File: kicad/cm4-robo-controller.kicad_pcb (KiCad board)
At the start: 4 copper layers, 150 x 90 mm, 254 parts, among them CN1 SMA-KWE_C7498154, J1 KF7620-7.62-2P, J10 KF2EDGR-2.54-2P, J11 KF7620-7.62-2P, J12 KF2EDGR-2.54-2P, J13 KF2EDGR-2.54-2P, J14 KF7620-7.62-2P, J15 PM254-2-12-Z-8.5, J16 PM254-2-09-Z-8.5, J2 HX PZ2.54-2X5P TP, J3 Header-Male-2.54_2x3, J4 2541WV-2X12P, J5 Header-Male-2.54_1x3, J6 Header-Male-2.54_2x3, J7 SMA-KWE_C7498154, J8 KF2EDGR-2.54-4P, J9 KF2EDGR-2.54-3P, Q1 SP40P04NK, Q2 DMP6023LE-13, Q3 NCE6008AS, Q4 BSS138, SW1 SS-12F49-G050, U1 74LVC1G07SE-7, U10 74LVC1G07SE-7, U11 MX26631DL, U12 MAX-M10S-00B, U13 74LVC1G17SE-7, U14 74LVC1G17SE-7, U15 AP64501SP-13, U16 74LVC1G17SE-7, U17 74LVC1G07SE-7, U18 TPS70933DBVR, U19 74LVC1G17SE-7, U2 FSUSB42MUX, U3 USB2514B-I/M2, U4 AP22653W6-7, U5 TPD4EUSB30DQAR, U6 TPD4EUSB30DQAR, U7 TPD4EUSB30DQAR, U8 TPD4EUSB30DQAR, U9 TPD4EUSB30DQAR, X1 24MHz

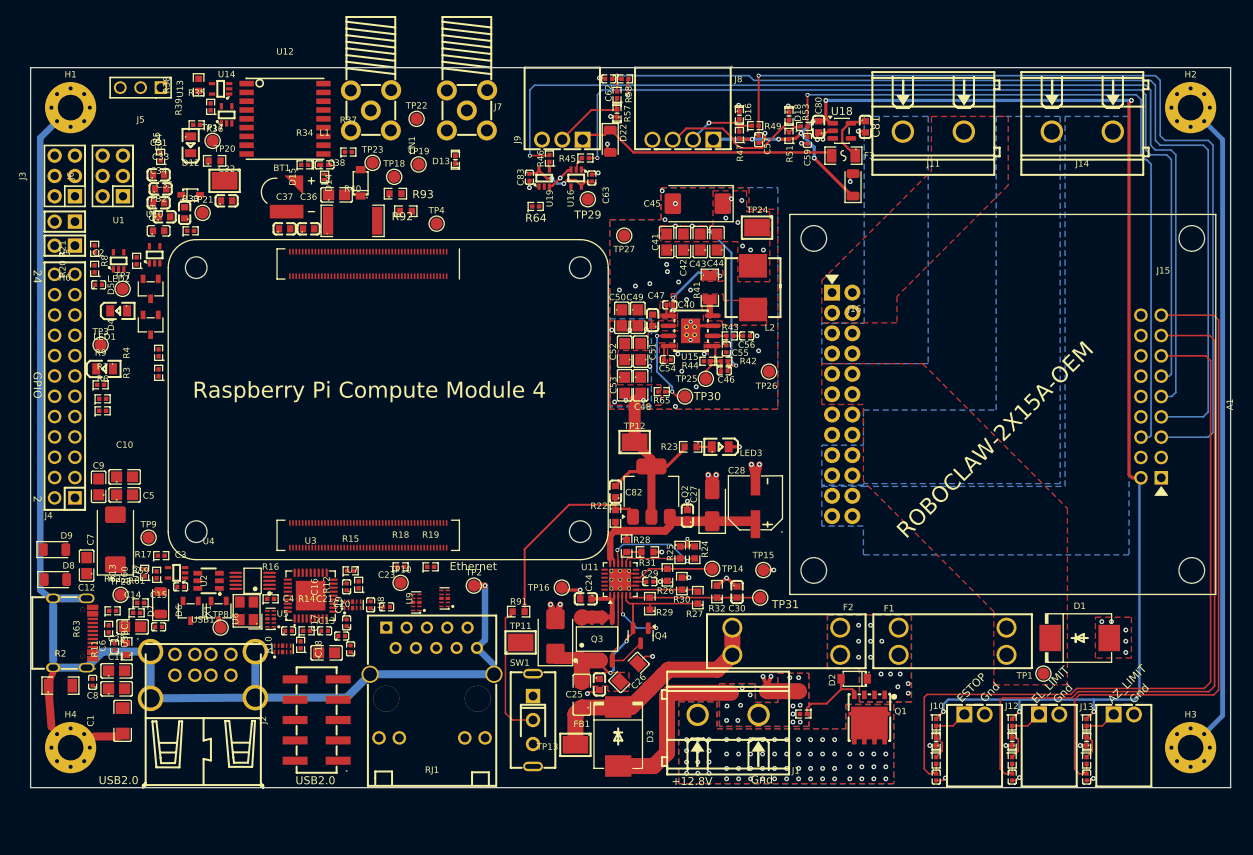
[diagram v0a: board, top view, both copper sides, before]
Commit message: PCB rework: rotate RoboClaw, battery input at top, planes redrawn, right half routed
- A1 rotated 90 CW and moved down; J14/J11 motor pours straight to the A1 pins
- J14 pins swapped (M2 polarity) in the schematic; J14 moved clear of D1
- Battery input, fuses and TVS diodes along the top edge; NT1 at J1-
- In1 (GND/PGND) and In2 (5V/V_MOTOR) split redrawn for the new layout
- Power block re-routed; 12V fed to the buck input on B.Cu
- UART buffers back on logic GND; RoboClaw signal section routed
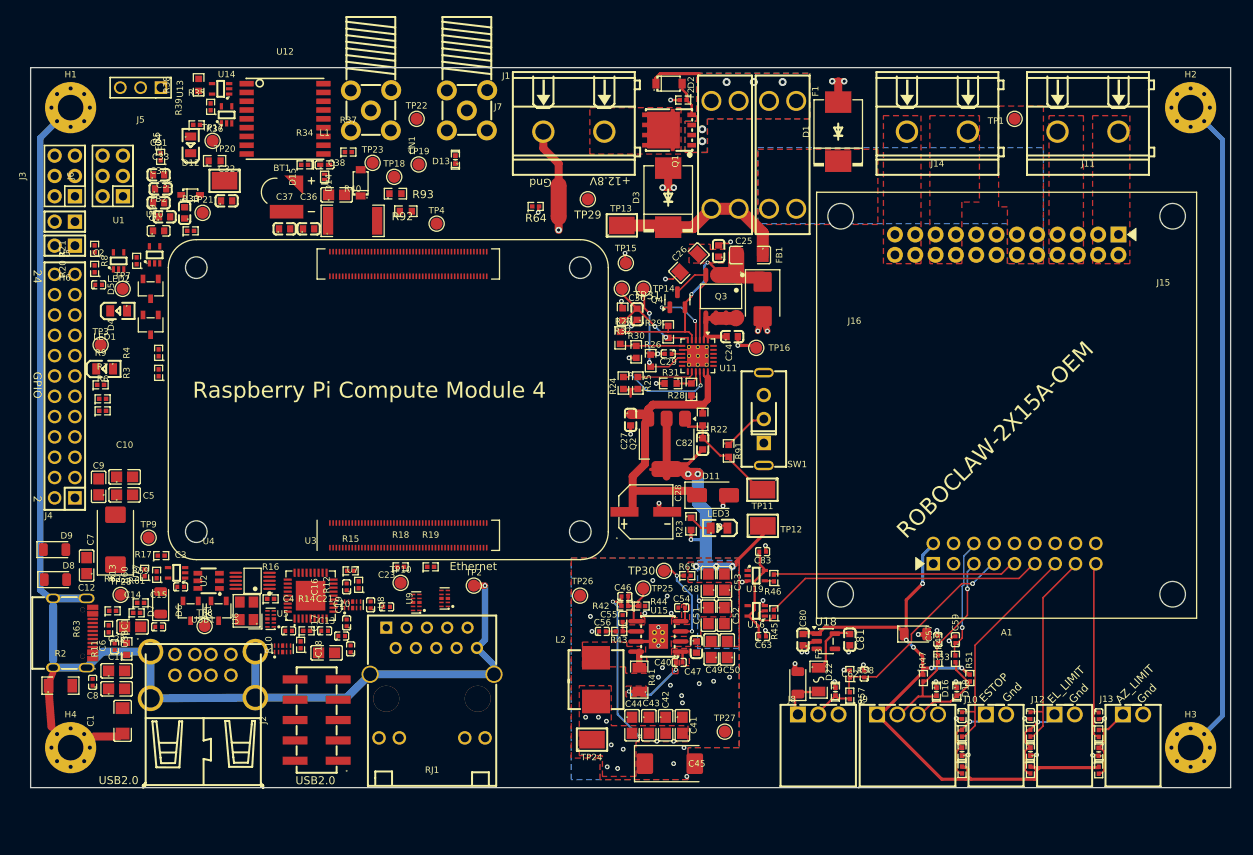
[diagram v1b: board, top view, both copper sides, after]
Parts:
- moved C62 81.0 mm to (164.2, 125.4), turned to 90 degrees
- moved R57 80.5 mm to (162.4, 128.1)
- moved R58 79.5 mm to (162.4, 125.4), turned to 90 degrees
- moved J9 78.7 mm to (158.5, 130.4), turned to 0 degrees
- moved R1 78.2 mm to (141.6, 53.6)
- moved D2 77.9 mm to (139.8, 51.6), turned to 0 degrees
- moved Q1 77.6 mm to (139.8, 57.4), turned to 90 degrees
- moved D22 77.3 mm to (160.6, 127.6), turned to -90 degrees
- moved J8 77.1 mm to (169.6, 130.4), turned to 0 degrees
- moved D16 76.1 mm to (173.2, 127.6)
- moved J1 75.4 mm to (127.9, 57.6), turned to 180 degrees
- moved D18 74.9 mm to (175.8, 127.6)
- moved R47 71.7 mm to (171.6, 125.9), turned to -90 degrees
- moved D23 71.6 mm to (155.9, 126.5), turned to 90 degrees
- moved R51 71.4 mm to (177.4, 125.9), turned to -90 degrees
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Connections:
- J14 pad 1: /Robo/M2A -> /Robo/M2B
- J14 pad 2: /Robo/M2B -> /Robo/M2A
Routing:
- net /Robo/EN1_A: track 114.0 -> 12.7 mm
- net Net-(A1-S1_RX): track 130.4 -> 30.0 mm, vias 1 -> 0
- net /Robo/RC_5V: track 174.4 -> 75.8 mm, vias 10 -> 5
- net /Robo/EN2_A: track 123.2 -> 25.4 mm
- net Net-(A1-S2_TX): track 116.1 -> 34.4 mm, vias 1 -> 0
- net /Robo/EN1_B: track 90.3 -> 14.3 mm
- net /Robo/ESTOP: track 95.1 -> 27.4 mm
- net /Robo/EL_LIMIT: track 89.2 -> 24.9 mm
- net /Robo/AZ_LIMIT: track 83.8 -> 22.0 mm
- net /Robo/AZ_ENC_3V3: track 30.8 -> 3.55 mm
- net /power/12V: track 21.0 -> 41.4 mm
- net Net-(Q2-G): track 25.0 -> 11.9 mm
- net GND: track 40.4 -> 27.9 mm, vias 42 -> 41
- net Net-(R91-Pad1): track 16.9 -> 5.00 mm
- net /power/EFUSE_OUT: track 26.4 -> 36.1 mm
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- added copper zone on F.Cu, net /Robo/M1B
- added copper zone on F.Cu, net /Robo/M2A
- added copper zone on F.Cu, net /Robo/M2B
- added copper zone on B.Cu, net /Robo/V_MOTOR
- removed copper zone on B.Cu, net /Robo/M1B
- removed copper zone on B.Cu, net /Robo/M2A
- removed copper zone on B.Cu, net /Robo/M2B
- removed copper zone on B.Cu, net Net-(J1-Pad1)
- removed copper zone on B.Cu, net PGND
- removed copper zone on F.Cu, net PGND

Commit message: PCB: place GPS and USB sheet components
GPS: RF chain (L1, D15) and antenna bias network at CN1, 1PPS input
chain (U13, R37/R38, C34, D13) by J7, backup cell row, LED and test
points grouped.

USB: ESD at each connector (U5 at USB-C, U6 at USB1, U7 at J2), VBUS
TVS at the ports, CC and VBUS-detect resistors at USBC1, hub crystal,
strap and decoupling parts tight around U3, MUX_OE parts by U2, port
power (U4 and caps) grouped by C7. TP8 moved to the left edge.

Reference labels normalized to 0.8 mm and placed clear of bodies.
Removed a dangling GND stub and via left by the old R64 position.
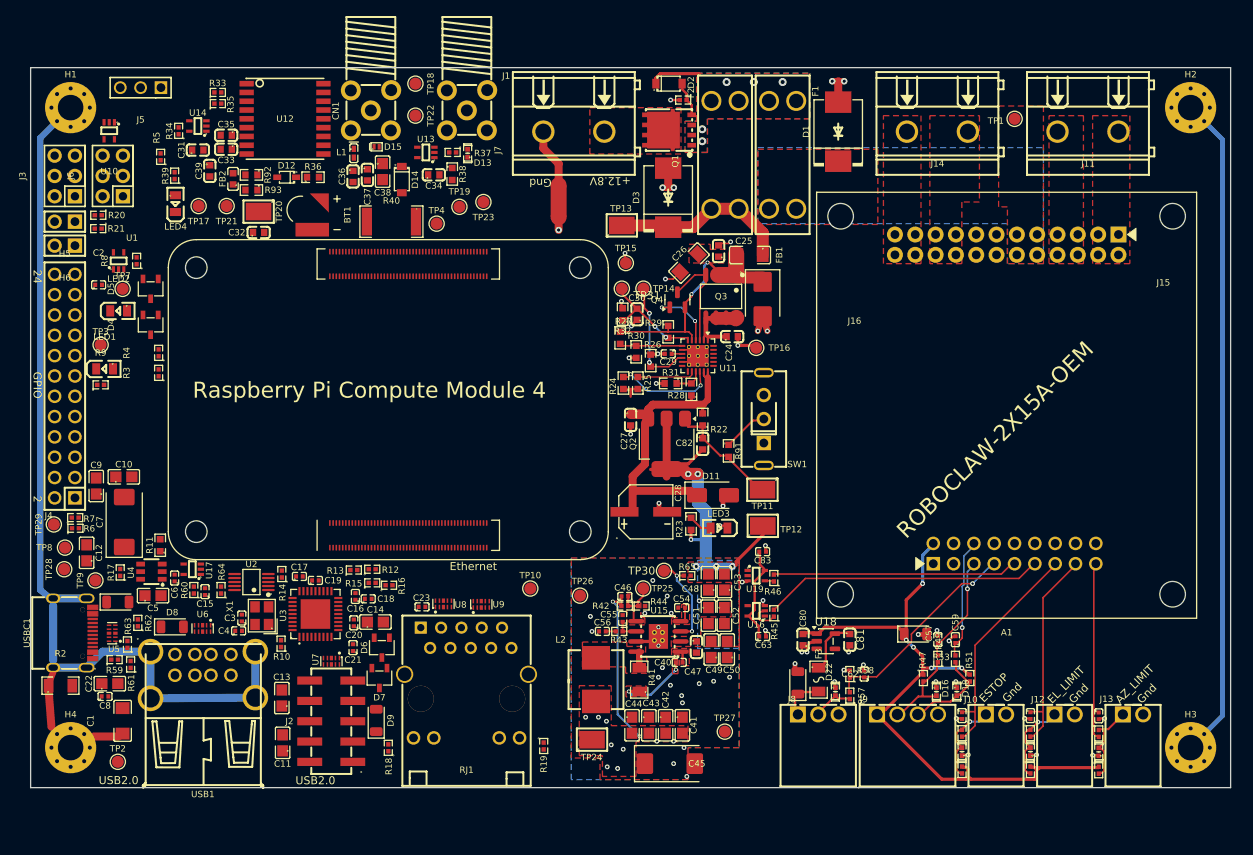
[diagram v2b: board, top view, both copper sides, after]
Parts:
- moved TP29 78.2 mm to (62.9, 106.7)
- moved R64 62.0 mm to (83.8, 114.9), turned to 90 degrees
- moved TP2 49.7 mm to (70.9, 136.4)
- moved D9 45.5 mm to (103.2, 131.2), turned to 90 degrees
- moved C34 34.6 mm to (110.4, 63.0)
- moved R38 33.6 mm to (112.7, 62.9), turned to -90 degrees
- moved C14 30.4 mm to (103.1, 118.9)
- moved U13 26.9 mm to (109.4, 60.2)
- moved R19 26.5 mm to (124.1, 134.4), turned to -90 degrees
- moved R13 26.2 mm to (100.4, 112.4), turned to 0 degrees
- moved D7 25.1 mm to (103.6, 125.9)
- moved R18 22.7 mm to (104.7, 134.6), turned to 90 degrees
- moved C11 21.8 mm to (91.5, 134.0), turned to 90 degrees
- moved U5 21.4 mm to (70.2, 120.3), turned to 90 degrees
- moved D6 20.9 mm to (103.9, 122.1)
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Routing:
- net CHASSIS: track 240.7 -> 195.9 mm, vias 1 -> 0
- net GND: track 27.9 -> 27.3 mm, vias 41 -> 40

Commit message: PCB: decoupling caps at IC supply pins, route GPS area
- Add 100nF decoupling for U10 (C84) and U17 (C85)
- Move C15, C18, C21, C25, C27, C32 next to their IC supply pins; shift R10
- Route the GPS section: RF_IN, antenna bias, GPS VCC, V_BCKP, local signals, GND/5V plane vias
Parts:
- added C84: 100nF, MyPartsIPC:CAPC1005X55N, F.Cu at (71.8, 58.6)
- added C85: 100nF, MyPartsIPC:CAPC1005X55N, F.Cu at (79.2, 114.5)
- moved C32 14.7 mm to (84.9, 55.9), turned to 90 degrees
- moved C27 11.8 mm to (145.8, 88.9), turned to 0 degrees
- moved C18 11.7 mm to (92.0, 121.7), turned to 180 degrees
- moved R9 11.4 mm to (73.5, 78.9)
- moved C25 10.4 mm to (140.9, 81.6)
- moved C15 9.50 mm to (91.3, 115.0), turned to 0 degrees
- moved TP3 9.45 mm to (73.8, 92.2)
- moved R8 4.88 mm to (68.9, 76.0), turned to 0 degrees
- moved C21 4.70 mm to (95.6, 122.3), turned to -90 degrees
- moved C2 4.43 mm to (68.9, 72.3)
- moved LED1 3.56 mm to (70.4, 83.9)
- moved R10 1.66 mm to (91.5, 120.0)
- moved LED2 0.81 mm to (70.3, 80.4)
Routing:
- net /GPS/VCC: track 0.00 -> 42.4 mm, vias 0 -> 2
- net /GPS/VCC_RF: track 0.00 -> 26.7 mm
- net /GPS/EXT_1PPS: track 0.00 -> 22.4 mm, vias 0 -> 2
- net /GPS/V_BCKP: track 0.00 -> 21.3 mm, vias 0 -> 2
- net GND: track 27.3 -> 44.6 mm, vias 40 -> 63
- net Net-(D14-K): track 0.00 -> 12.9 mm
- net /CM4/GPS_TX_MCU: track 0.00 -> 11.3 mm
- net Net-(U12-SAFEBOOT_N): track 0.00 -> 11.2 mm
- net /GPS/RF_IN: track 0.00 -> 9.12 mm
- net /GPS/PPS_BUF: track 0.00 -> 7.13 mm
- net Net-(D13-A): track 0.00 -> 5.32 mm
- net /GPS/TIMEPULSE: track 0.00 -> 5.05 mm, vias 0 -> 2
- net /GPS/Net-(LED2-A): track 0.00 -> 4.46 mm
- net Net-(D12-A): track 0.00 -> 3.45 mm, vias 0 -> 2
- net Net-(U13-A): track 0.00 -> 3.36 mm
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
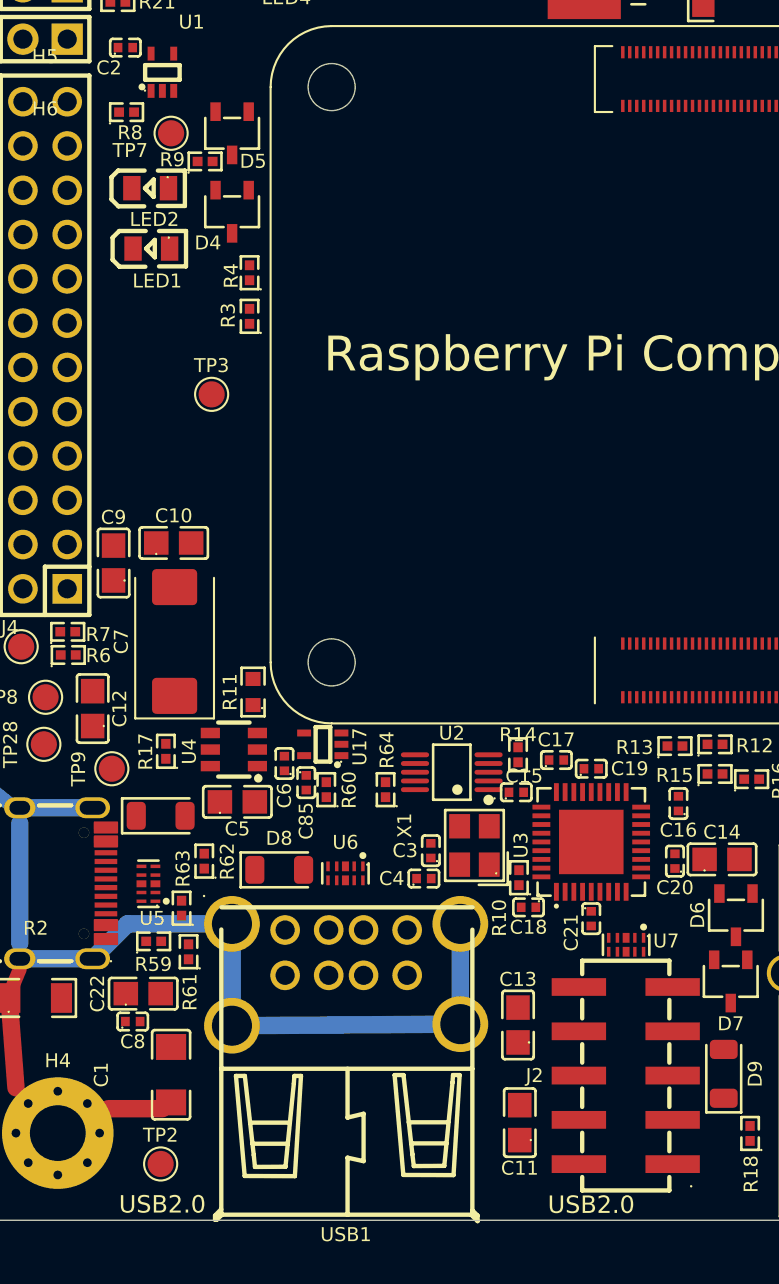
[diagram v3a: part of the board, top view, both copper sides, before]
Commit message: PCB: route the USB differential pairs
- HD1-HD4, hub upstream, USB2 to CM4 and HSD2 to USB-C routed as 90 ohm pairs
- ESD parts (U5/U6/U7) routed flow-through: used N.C. pins tied to their lines
- Swap hub ports at J2 (HD3<->HD4) and USB1 (HD1<->HD2) to avoid pair crossings
- Move U6, U5, R63, R64, R14, C15, C18 to make room for the escapes
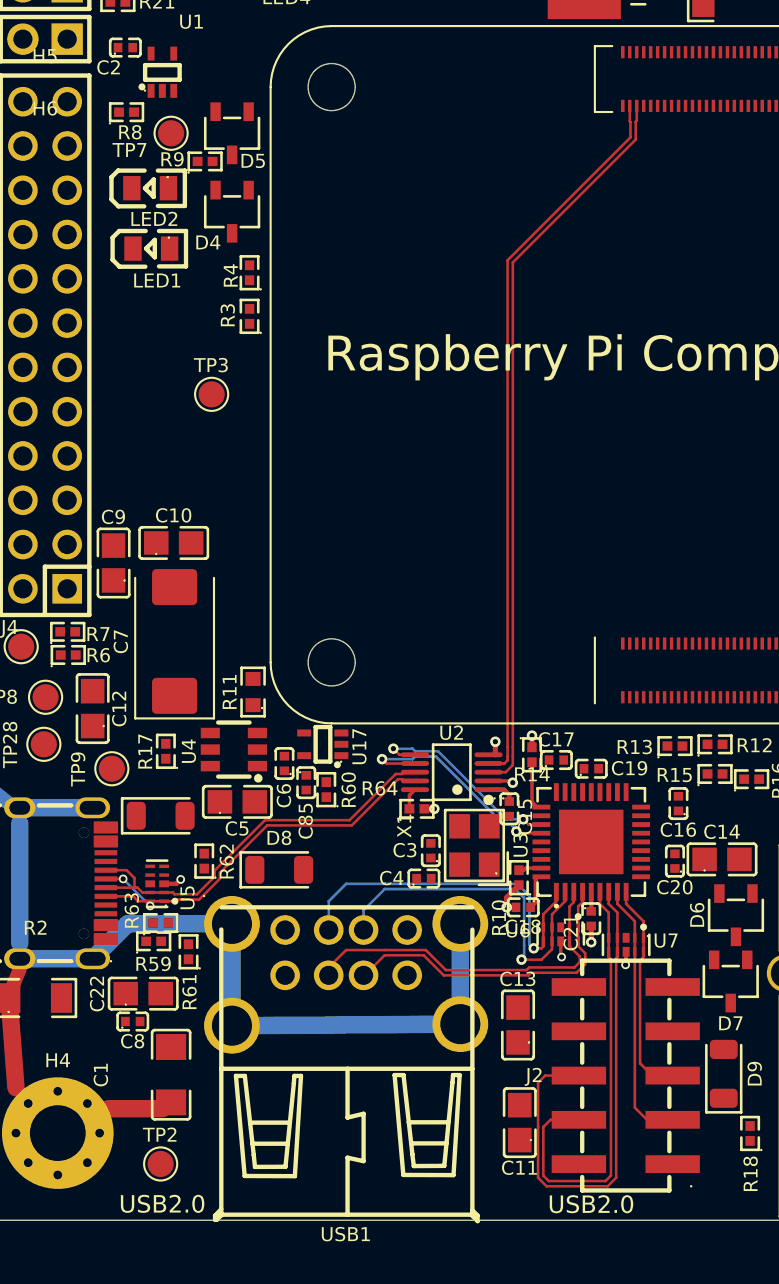
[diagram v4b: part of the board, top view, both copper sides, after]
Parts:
- moved U6 12.8 mm to (93.8, 123.2)
- moved R64 2.11 mm to (85.6, 116.0), turned to 0 degrees
- moved R63 1.47 mm to (70.9, 122.5), turned to 0 degrees
- moved C15 1.03 mm to (90.9, 116.0), turned to -90 degrees
- moved R14 0.80 mm to (92.2, 112.9), turned to -90 degrees
- moved U5 0.50 mm to (70.7, 120.3)
- moved C18 0.30 mm to (91.7, 121.7)
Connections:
- J2 pad 3: /CM4/usb/HD3_N -> /CM4/usb/HD4_N
- J2 pad 4: /CM4/usb/HD4_N -> /CM4/usb/HD3_N
- J2 pad 5: /CM4/usb/HD3_P -> /CM4/usb/HD4_P
- J2 pad 6: /CM4/usb/HD4_P -> /CM4/usb/HD3_P
- U5 pad 10: unconnected-(U5-N.C.-Pad10) -> /CM4/usb/HSD2+
- U5 pad 9: unconnected-(U5-N.C.-Pad9) -> /CM4/usb/HSD2-
- U6 pad 10: unconnected-(U6-N.C.-Pad10) -> /CM4/usb/HD2_P
- U6 pad 6: unconnected-(U6-N.C.-Pad6) -> /CM4/usb/HD1_N
- U6 pad 7: unconnected-(U6-N.C.-Pad7) -> /CM4/usb/HD1_P
- U6 pad 9: unconnected-(U6-N.C.-Pad9) -> /CM4/usb/HD2_N
- U7 pad 10: unconnected-(U7-N.C.-Pad10) -> /CM4/usb/HD4_P
- U7 pad 6: unconnected-(U7-N.C.-Pad6) -> /CM4/usb/HD3_N
- U7 pad 7: unconnected-(U7-N.C.-Pad7) -> /CM4/usb/HD3_P
- U7 pad 9: unconnected-(U7-N.C.-Pad9) -> /CM4/usb/HD4_N
- USB1 pad 2: /CM4/usb/HD2_N -> /CM4/usb/HD1_N
- USB1 pad 3: /CM4/usb/HD2_P -> /CM4/usb/HD1_P
- USB1 pad 6: /CM4/usb/HD1_N -> /CM4/usb/HD2_N
- USB1 pad 7: /CM4/usb/HD1_P -> /CM4/usb/HD2_P
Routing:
- net /CM4/USB2_P: track 0.00 -> 42.3 mm
- net /CM4/USB2_N: track 0.00 -> 41.6 mm
- net /CM4/usb/HD3_P: track 0.00 -> 29.5 mm
- net /CM4/usb/HD3_N: track 0.00 -> 25.7 mm
- net /CM4/usb/HSD2+: track 0.00 -> 24.2 mm, vias 0 -> 2
- net /CM4/usb/HSD2-: track 0.00 -> 23.4 mm
- net /CM4/usb/HD1_N: track 0.00 -> 21.0 mm, vias 0 -> 1
- net /CM4/usb/HD2_N: track 0.00 -> 20.3 mm
- net /CM4/usb/HD1_P: track 0.00 -> 20.3 mm, vias 0 -> 1
- net /CM4/usb/HD2_P: track 0.00 -> 18.4 mm
- net /CM4/usb/HD4_N: track 0.00 -> 15.3 mm
- net /CM4/usb/USB_HUB_P: track 0.00 -> 13.1 mm, vias 0 -> 2
- net /CM4/usb/HD4_P: track 0.00 -> 12.5 mm
- net /CM4/usb/USB_HUB_N: track 0.00 -> 11.7 mm, vias 0 -> 2
- net GND: track 44.6 -> 52.9 mm, vias 63 -> 71
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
